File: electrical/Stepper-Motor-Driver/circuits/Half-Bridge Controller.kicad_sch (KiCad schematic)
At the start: 16 parts, among them Q3 IRF530NPBF, Q4 IRF530NPBF, U1 UCC27710D

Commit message: Current sensing circuit
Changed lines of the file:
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@@
 	(wire
 		(pts
-			(xy 132.08 36.83) (xy 132.08 35.56)
+			(xy 100.33 54.61) (xy 119.38 54.61)
 		)
 		(stroke
@@
 	(wire
 		(pts
-			(xy 100.33 54.61) (xy 119.38 54.61)
+			(xy 36.83 45.72) (xy 40.64 45.72)
 		)
 		(stroke
@@
 	(wire
 		(pts
-			(xy 36.83 45.72) (xy 40.64 45.72)
+			(xy 119.38 53.34) (xy 119.38 54.61)
 		)
 		(stroke
@@
 	(wire
 		(pts
-			(xy 119.38 53.34) (xy 119.38 54.61)
+			(xy 100.33 50.8) (xy 100.33 54.61)
 		)
 		(stroke
@@
 	(wire
 		(pts
-			(xy 100.33 50.8) (xy 100.33 54.61)
+			(xy 119.38 54.61) (xy 132.08 54.61)
 		)
 		(stroke
@@
 	(wire
 		(pts
-			(xy 119.38 54.61) (xy 132.08 54.61)
+			(xy 132.08 54.61) (xy 132.08 62.23)
 		)
 		(stroke
@@
 		)
 	)
-	(wire
-		(pts
-			(xy 132.08 54.61) (xy 132.08 62.23)
-		)
-		(stroke
-			(width 0)
-			(type default)
-		)
-	)
 	(hierarchical_label "OUT"
-		(shape input)
+		(shape bidirectional)
 		(at 135.89 54.61 0)
 		(effects
@@
 	(symbol
 		(lib_id "power:+24V")
-		(at 132.08 35.56 0)
+		(at 132.08 36.83 0)
 		(unit 1)
 		(body_style 1)
@@
 		(fields_autoplaced yes)
 		(property "Reference" "#PWR02"
-			(at 132.08 39.37 0)
+			(at 132.08 40.64 0)
 			(hide yes)
 			(show_name no)
@@
 		)
 		(property "Value" "+24V"
-			(at 132.08 30.48 0)
+			(at 132.08 31.75 0)
 			(show_name no)
 			(do_not_autoplace no)
@@
 		)
 		(property "Footprint" ""
-			(at 132.08 35.56 0)
+			(at 132.08 36.83 0)
 			(hide yes)
 			(show_name no)
@@
 		)
 		(property "Datasheet" ""
-			(at 132.08 35.56 0)
+			(at 132.08 36.83 0)
 			(hide yes)
 			(show_name no)
@@
 		)
 		(property "Description" "Power symbol creates a global label with name \"+24V\""
-			(at 132.08 35.56 0)
-			(hide yes)
-			(show_name no)
+			(at 132.08 36.83 0)
+			(hide yes)
+			(show_name no)

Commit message: Symbol cleanup and initial power section design
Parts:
- C5, C8: footprint (none) -> Capacitor_SMD:C_1206_3216Metric
- Q3, Q4: footprint IRF530NPBF:TO254P1041X444X1930-3 -> IRF530NPBF:IRF530NPBF
- R13, R16, R19, R21, R22, R23, R27, R29: footprint (none) -> Resistor_SMD:R_1206_3216Metric
- U1: footprint D0008B_N -> UCC27710D:UCC27710D
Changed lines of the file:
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@@
 			)
 		)
-		(property "Footprint" ""
+		(property "Footprint" "Resistor_SMD:R_1206_3216Metric"
 			(at 107.95 37.592 90)
 			(hide yes)
@@
 			)
 		)
-		(property "Footprint" ""
+		(property "Footprint" "Resistor_SMD:R_1206_3216Metric"
 			(at 104.14 68.072 90)
 			(hide yes)
@@
 			)
 		)
-		(property "Footprint" "D0008B_N"
+		(property "Footprint" "UCC27710D:UCC27710D"
 			(at 71.12 48.26 0)
 			(hide yes)
@@
 			)
 		)
-		(property "Footprint" ""
+		(property "Footprint" "Resistor_SMD:R_1206_3216Metric"
 			(at 100.33 61.722 90)
 			(hide yes)
@@
 			)
 		)
-		(property "Footprint" "IRF530NPBF:TO254P1041X444X1930-3"
+		(property "Footprint" "IRF530NPBF:IRF530NPBF"
 			(at 129.54 41.91 0)
 			(hide yes)
@@
 			)
 		)
-		(property "Footprint" ""
+		(property "Footprint" "Capacitor_SMD:C_1206_3216Metric"
 			(at 33.02 39.0652 0)
 			(hide yes)
@@
 			)
 		)
-		(property "Footprint" ""
+		(property "Footprint" "Resistor_SMD:R_1206_3216Metric"
 			(at 117.602 49.53 90)
 			(hide yes)
@@
 			)
 		)
-		(property "Footprint" ""
+		(property "Footprint" "Resistor_SMD:R_1206_3216Metric"
 			(at 111.76 46.228 90)
 			(hide yes)
@@
 			)
 		)
-		(property "Footprint" ""
+		(property "Footprint" "Resistor_SMD:R_1206_3216Metric"
 			(at 38.862 41.91 90)
 			(hide yes)
@@
 			)
 		)
-		(property "Footprint" "IRF530NPBF:TO254P1041X444X1930-3"
+		(property "Footprint" "IRF530NPBF:IRF530NPBF"
 			(at 129.54 67.31 0)
 			(hide yes)
@@
 			)
 		)
-		(property "Footprint" ""
+		(property "Footprint" "Resistor_SMD:R_1206_3216Metric"
 			(at 69.85 32.258 90)
 			(hide yes)
@@
 			)
 		)
-		(property "Footprint" ""
+		(property "Footprint" "Capacitor_SMD:C_1206_3216Metric"
 			(at 101.2952 48.26 0)
 			(hide yes)
@@
 			)
 		)
-		(property "Footprint" ""
+		(property "Footprint" "Resistor_SMD:R_1206_3216Metric"
 			(at 109.982 73.66 90)
 			(hide yes)

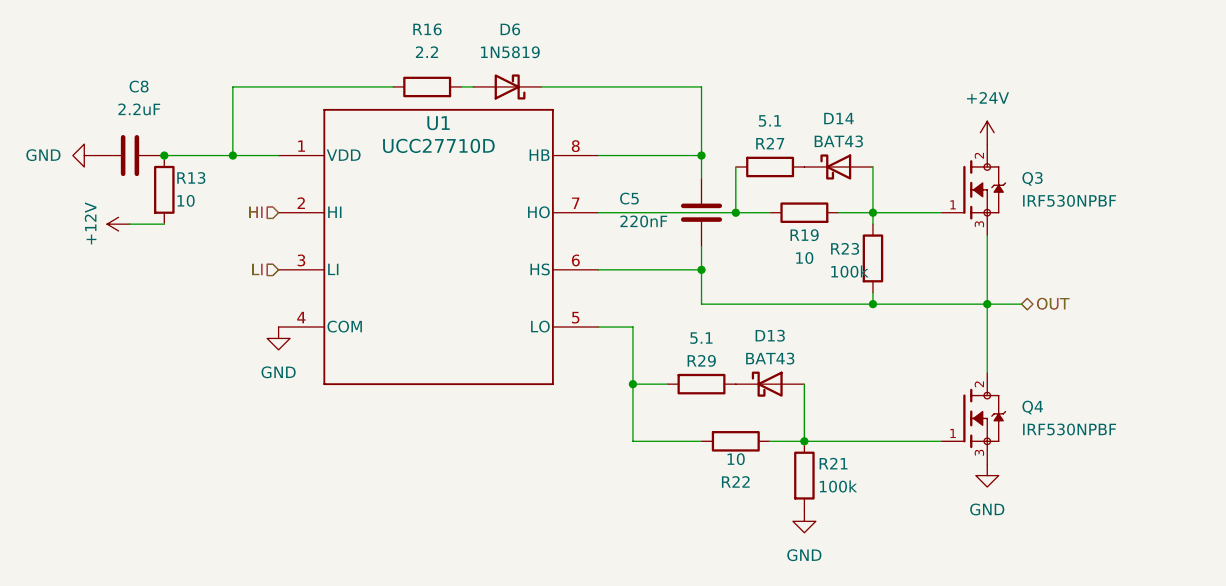
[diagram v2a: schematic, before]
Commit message: Fixed missing PWR_FLAG
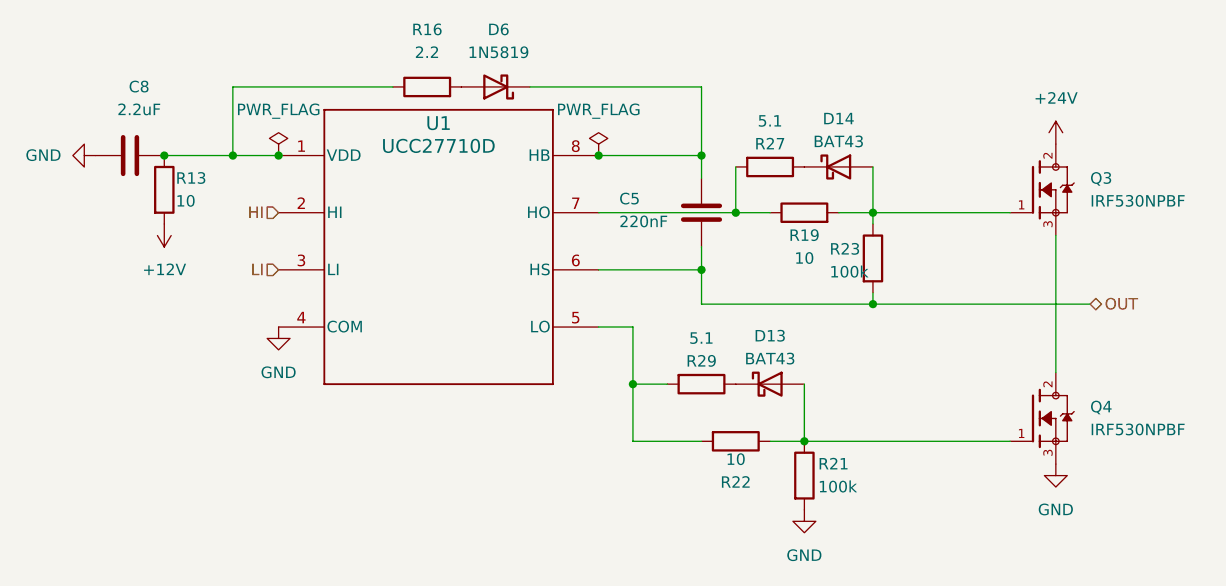
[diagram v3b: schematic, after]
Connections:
- net OUT: no longer Q3.3, Q4.2
- new net: Q3.3, Q4.2
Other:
- moved on the sheet: D6, Q3, Q4

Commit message: Fixed missing connection
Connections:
- net OUT: now also Q3.3, Q4.2
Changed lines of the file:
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@@
 	(paper "A4")
 	(junction
+		(at 92.71 63.5)
+		(diameter 0)
+		(color 0 0 0 0)
+	)
+	(junction
 		(at 119.38 54.61)
 		(diameter 0)
@@
 	)
 	(junction
-		(at 92.71 63.5)
-		(diameter 0)
-		(color 0 0 0 0)
-	)
-	(junction
 		(at 40.64 38.1)
 		(diameter 0)
@@
 		(color 0 0 0 0)
 	)
+	(junction
+		(at 139.7 54.61)
+		(diameter 0)
+		(color 0 0 0 0)
+	)
 	(wire
 		(pts
@@
 	(wire
 		(pts
+			(xy 119.38 54.61) (xy 139.7 54.61)
+		)
+		(stroke
+			(width 0)
+			(type default)
+		)
+	)
+	(wire
+		(pts
 			(xy 119.38 39.37) (xy 119.38 44.45)
 		)
@@
 	(wire
 		(pts
-			(xy 139.7 46.99) (xy 139.7 62.23)
+			(xy 139.7 46.99) (xy 139.7 54.61)
 		)
 		(stroke
@@
 	(wire
 		(pts
+			(xy 139.7 54.61) (xy 139.7 62.23)
+		)
+		(stroke
+			(width 0)
+			(type default)
+		)
+	)
+	(wire
+		(pts
 			(xy 100.33 48.26) (xy 100.33 50.8)
 		)
@@
 	(wire
 		(pts
+			(xy 139.7 54.61) (xy 143.51 54.61)
+		)
+		(stroke
+			(width 0)
+			(type default)
+		)
+	)
+	(wire
+		(pts
 			(xy 100.33 54.61) (xy 119.38 54.61)
 		)
@@
 		)
 		(stroke
-			(width 0)
-			(type default)
-		)
-	)
-	(wire
-		(pts
-			(xy 119.38 54.61) (xy 143.51 54.61)
-		)
-		(stroke

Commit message: Adding test points and FPGA sockets
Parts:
- added TP1, TP13, TP5, TP9: TestPoint, Connector_PinHeader_1.00mm:PinHeader_1x01_P1.00mm_Vertical, symbol Connector:TestPoint
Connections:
- net OUT: now also TP5.1
- net at D14.2 (A), Q3.1, R19.2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: now also TP1.1
- net at D13.2 (A), Q4.1, R21.1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: now also TP9.1
- net at C5.1, D6.1 (K), U1.8 (HB): now also TP13.1

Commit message: Initial PCB layout
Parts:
- renumbered C5 to C10, C8 to C9, D6 to D1, D13 to D2, D14 to D3, Q3 to Q1, Q4 to Q2, R16 to R10, R29 to R11, R22 to R12, R27 to R13, R19 to R14, R21 to R15, R23 to R16, R13 to R9, TP13 to TP1, TP1 to TP2, TP5 to TP3, TP9 to TP4, U1 to U2
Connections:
- net +24V renamed +VMotorIn
